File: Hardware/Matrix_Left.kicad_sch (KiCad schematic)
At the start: 0 parts

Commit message: Schematic review
Initial shcematic iteration.
Added all footprints and part numbers.
Only a quick review was performed.
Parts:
- added C13, C14, C15, C16, C17, C18, C19, C20, C21, C22, C23, C24, C25, C26, C27, C28, C29, C30, C31, C32, C33, C34, C35, C36, C37, C38, C39, C40, C41, C42, C43, C44, C45, C46, C47: 1u, Capacitor_SMD:C_0603_1608Metric, symbol Device:C
- added D10, D11, D17, D18, D19, D20, D21, D27, D28, D29, D30, D31, D37, D38, D39, D40, D41, D47, D48, D50, D51, D52, D57, D58, D60, D61, D62, D67, D68, D69, D7, D70, D71, D8, D9: SK6812MINI-E, LED_SMD:LED_SK6812MINI-E_3.2x2.8mm_P1.5mm_ReverseMount, symbol LED:SK6812MINI-E
- added D12, D13, D14, D15, D16, D22, D23, D24, D25, D26, D32, D33, D34, D35, D36, D42, D43, D44, D45, D46, D49, D53, D54, D55, D56, D59, D63, D64, D65, D66, D72, D73, D74, D75, D76: 1N4148WT, Diode_SMD:D_SOD-523, symbol Diode:1N4148WT
- added SW10, SW11, SW12, SW13, SW14, SW15, SW16, SW17, SW18, SW19, SW20, SW21, SW22, SW23, SW24, SW25, SW26, SW27, SW28, SW29, SW3, SW30, SW31, SW32, SW33, SW34, SW4, SW5, SW6, SW7, SW8, SW9: PG1350, Custom_Parts:PG1350_1.00u_PCB, symbol Switch:SW_Push
- added SW35: ENCODER, Custom_Parts:ALPS_EC11J_ENCODER, symbol Device:RotaryEncoder_Switch_MP
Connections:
- new net: D73.2 (A), SW32.2
- new net: D46.2 (A), SW22.2
- new net: D75.2 (A), SW34.2
- new net: D55.2 (A), SW25.2
- new net: D33.2 (A), SW14.2
- new net: D34.2 (A), SW15.2
- new net: D39.4 (DOUT), D50.2 (DIN)
- new net: D50.4 (DOUT), D60.2 (DIN)
- new net: D32.2 (A), SW13.2
- new net: D15.2 (A), SW6.2
- new net: D62.4 (DOUT), D71.2 (DIN)
- new net: D25.2 (A), SW11.2
- new net: D63.2 (A), SW27.2
- new net: D45.2 (A), SW21.2
- new net: D18.2 (DIN), D28.4 (DOUT)
- new net: D18.4 (DOUT), D8.2 (DIN)
- new net: D21.4 (DOUT), D31.2 (DIN)
- new net: D31.4 (DOUT), D41.2 (DIN)
- new net: D56.2 (A), SW26.2
- new net: D23.2 (A), SW9.2
- new net: D47.2 (DIN), D57.4 (DOUT)
- new net: D37.2 (DIN), D47.4 (DOUT)
- new net: D42.2 (A), SW18.2
- new net: D10.2 (DIN), D7.4 (DOUT)
- new net: D10.4 (DOUT), D20.2 (DIN)
- new net: D60.4 (DOUT), D69.2 (DIN)
- new net: D26.2 (A), SW12.2
- new net: D43.2 (A), SW19.2
- new net: D65.2 (A), SW29.2
- new net: D74.2 (A), SW33.2
- new net: D67.2 (DIN), D69.4 (DOUT)
- new net: D16.2 (A), SW7.2
- new net: D12.2 (A), SW3.2
- new net: D30.4 (DOUT), D40.2 (DIN)
- new net: D40.4 (DOUT), D51.2 (DIN)
- new net: D57.2 (DIN), D67.4 (DOUT)
- new net: D27.2 (DIN), D37.4 (DOUT)
- new net: D41.4 (DOUT), D52.2 (DIN)
- new net: D20.4 (DOUT), D30.2 (DIN)
- new net: D51.4 (DOUT), D61.2 (DIN)
- new net: D61.4 (DOUT), D70.2 (DIN)
- new net: D58.2 (DIN), D68.4 (DOUT)
- new net: D48.2 (DIN), D58.4 (DOUT)
- new net: D66.2 (A), SW30.2
- new net: D14.2 (A), SW5.2
- new net: D35.2 (A), SW16.2
- new net: D38.2 (DIN), D48.4 (DOUT)
- new net: D28.2 (DIN), D38.4 (DOUT)
- new net: D11.2 (DIN), D8.4 (DOUT)
- new net: D11.4 (DOUT), D21.2 (DIN)
- new net: D13.2 (A), SW4.2
- new net: D36.2 (A), SW17.2
- new net: D64.2 (A), SW28.2
- new net: D53.2 (A), SW23.2
- new net: D24.2 (A), SW10.2
- new net: D52.4 (DOUT), D62.2 (DIN)
- new net: D22.2 (A), SW8.2
- new net: D54.2 (A), SW24.2
- new net: D19.2 (DIN), D9.4 (DOUT)
- new net: D19.4 (DOUT), D29.2 (DIN)
- new net: D68.2 (DIN), D70.4 (DOUT)
- new net: D29.4 (DOUT), D39.2 (DIN)
- new net: D44.2 (A), SW20.2
- new net: D17.2 (DIN), D27.4 (DOUT)
- new net: D17.4 (DOUT), D7.2 (DIN)
- new net: D72.2 (A), SW31.2
- new net 5VL: C13.1, C14.1, C15.1, C16.1, C17.1, C18.1, C19.1, C20.1, C21.1, C22.1, C23.1, C24.1, C25.1, C26.1, C27.1, C28.1, C29.1, C30.1, C31.1, C32.1, C33.1, C34.1, C35.1, C36.1, C37.1, C38.1, C39.1, C40.1, C41.1, C42.1, C43.1, C44.1, C45.1, C46.1, C47.1, D10.3 (VDD), D11.3 (VDD), D17.3 (VDD), D18.3 (VDD), D19.3 (VDD), D20.3 (VDD), D21.3 (VDD), D27.3 (VDD), D28.3 (VDD), D29.3 (VDD), D30.3 (VDD), D31.3 (VDD), D37.3 (VDD), D38.3 (VDD), D39.3 (VDD), D40.3 (VDD), D41.3 (VDD), D47.3 (VDD), D48.3 (VDD), D50.3 (VDD), D51.3 (VDD), D52.3 (VDD), D57.3 (VDD), D58.3 (VDD), D60.3 (VDD), D61.3 (VDD), D62.3 (VDD), D67.3 (VDD), D68.3 (VDD), D69.3 (VDD), D7.3 (VDD), D70.3 (VDD), D71.3 (VDD), D8.3 (VDD), D9.3 (VDD)
- new net COL1_L: SW3.1, SW4.1, SW5.1, SW6.1, SW7.1
- new net COL2_L: SW10.1, SW11.1, SW12.1, SW8.1, SW9.1
- new net COL3_L: SW13.1, SW14.1, SW15.1, SW16.1, SW17.1
- new net COL4_L: SW18.1, SW19.1, SW20.1, SW21.1, SW22.1
- new net COL5_L: D49.2 (A), SW23.1, SW24.1, SW25.1, SW26.1
- new net COL6_L: D59.2 (A), SW27.1, SW28.1, SW29.1, SW30.1
- new net COL7_L: SW31.1, SW32.1, SW33.1, SW34.1, SW35.S1
- new net ENC_CC: D59.1 (K), SW35.B
- new net ENC_CW: D49.1 (K), SW35.A
- new net ENC_SW: D76.2 (A), SW35.S2
- new net GND: C13.2, C14.2, C15.2, C16.2, C17.2, C18.2, C19.2, C20.2, C21.2, C22.2, C23.2, C24.2, C25.2, C26.2, C27.2, C28.2, C29.2, C30.2, C31.2, C32.2, C33.2, C34.2, C35.2, C36.2, C37.2, C38.2, C39.2, C40.2, C41.2, C42.2, C43.2, C44.2, C45.2, C46.2, C47.2, D10.1 (VSS), D11.1 (VSS), D17.1 (VSS), D18.1 (VSS), D19.1 (VSS), D20.1 (VSS), D21.1 (VSS), D27.1 (VSS), D28.1 (VSS), D29.1 (VSS), D30.1 (VSS), D31.1 (VSS), D37.1 (VSS), D38.1 (VSS), D39.1 (VSS), D40.1 (VSS), D41.1 (VSS), D47.1 (VSS), D48.1 (VSS), D50.1 (VSS), D51.1 (VSS), D52.1 (VSS), D57.1 (VSS), D58.1 (VSS), D60.1 (VSS), D61.1 (VSS), D62.1 (VSS), D67.1 (VSS), D68.1 (VSS), D69.1 (VSS), D7.1 (VSS), D70.1 (VSS), D71.1 (VSS), D8.1 (VSS), D9.1 (VSS), SW35.MP
- new net LED_DATA_L: D9.2 (DIN)
- new net ROW1_L: D12.1 (K), D22.1 (K), D32.1 (K), D42.1 (K), D53.1 (K), D63.1 (K), D72.1 (K)
- new net ROW2_L: D13.1 (K), D23.1 (K), D33.1 (K), D43.1 (K), D54.1 (K), D64.1 (K), D73.1 (K)
- new net ROW3_L: D14.1 (K), D24.1 (K), D34.1 (K), D44.1 (K), D55.1 (K), D65.1 (K), D74.1 (K)
- new net ROW4_L: D15.1 (K), D25.1 (K), D35.1 (K), D45.1 (K), D56.1 (K), D66.1 (K), D75.1 (K)
- new net ROW5_L: D16.1 (K), D26.1 (K), D36.1 (K), D46.1 (K), D76.1 (K), SW35.C
- no-connect marks 0 -> 1

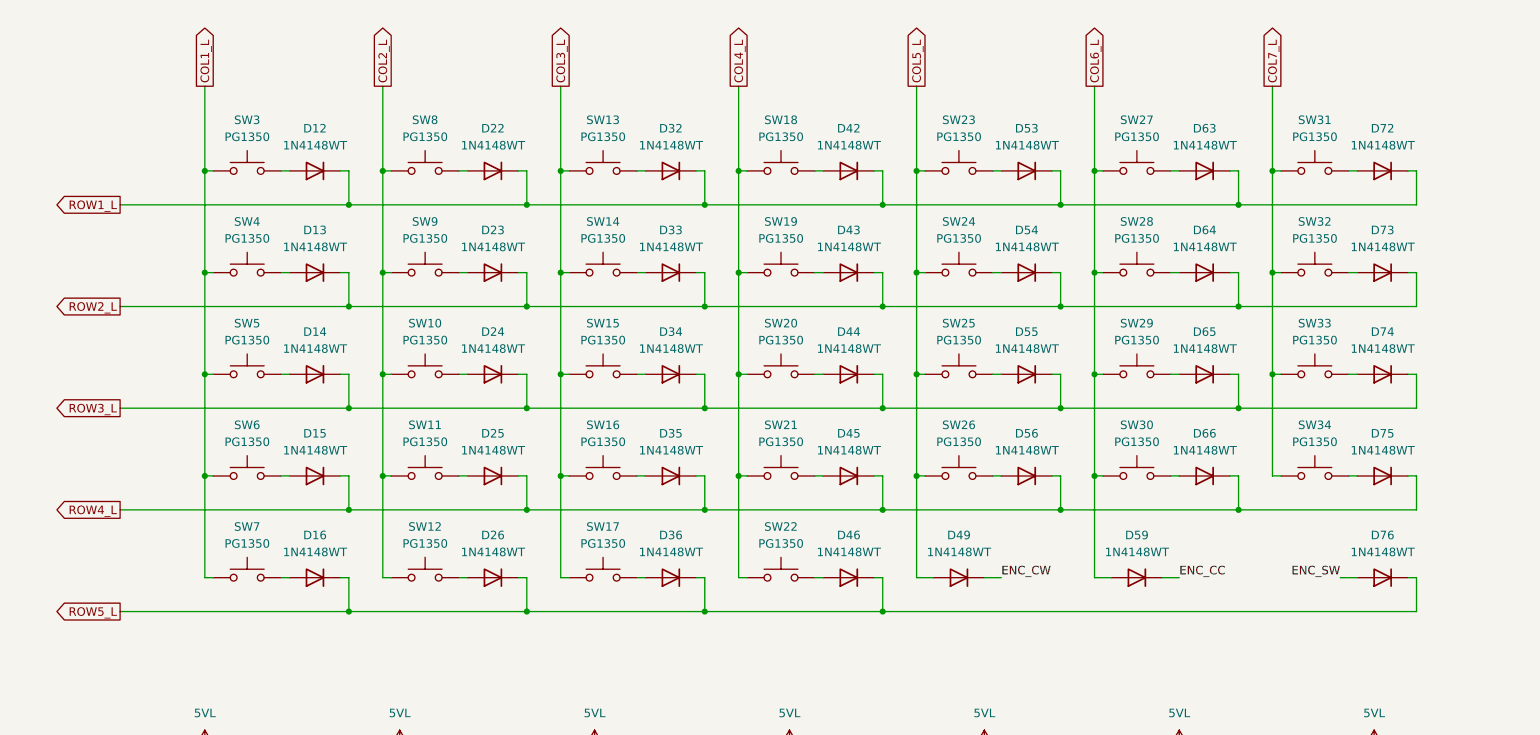
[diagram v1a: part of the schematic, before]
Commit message: Net configurations
Added net labels.
Updated the PCB components.
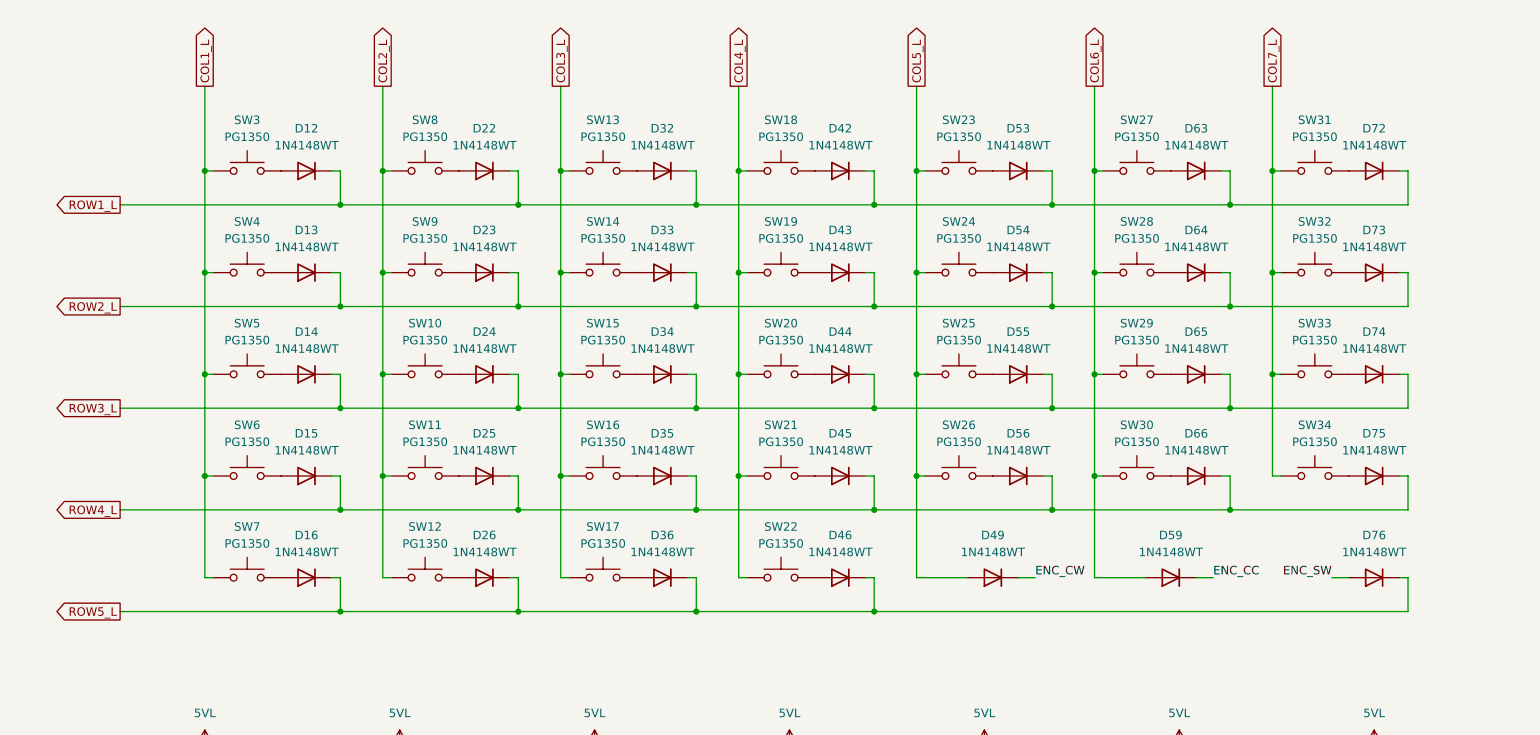
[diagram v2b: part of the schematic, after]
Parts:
- D10, D11, D17, D18, D19, D20, D21, D27, D28, D29, D30, D31, D37, D38, D39, D40, D41, D47, D48, D50, D51, D52, D57, D58, D60, D61, D62, D67, D68, D69, D7, D70, D71, D8, D9: footprint LED_SMD:LED_SK6812MINI-E_3.2x2.8mm_P1.5mm_ReverseMount -> Custom_Parts:LED_SK6812MINI-E_3.2x2.8mm_P1.5mm_ReverseMount
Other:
- moved on the sheet: D12, D13, D14, D15, D16, D22, D23, D24, D25, D26, D32, D33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

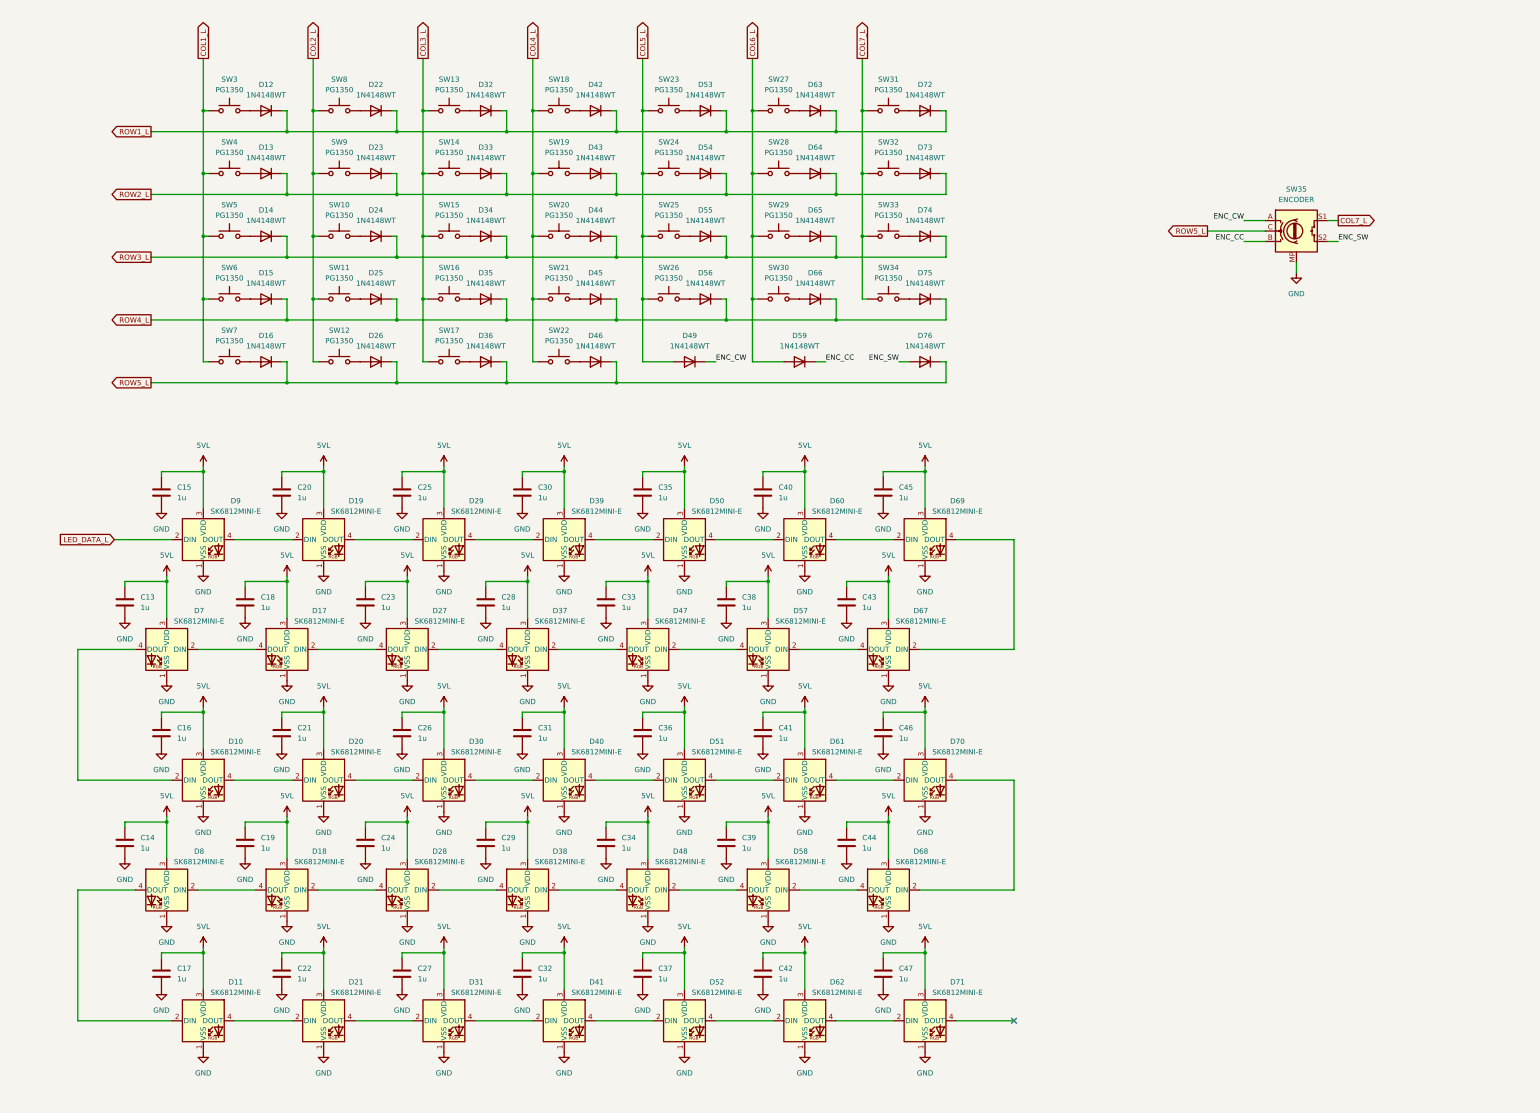
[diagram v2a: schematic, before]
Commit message: Initial layout
Configured the switch and LED initial layout.
Need to add the capacitors for the LEDs and the diodes for the switches.
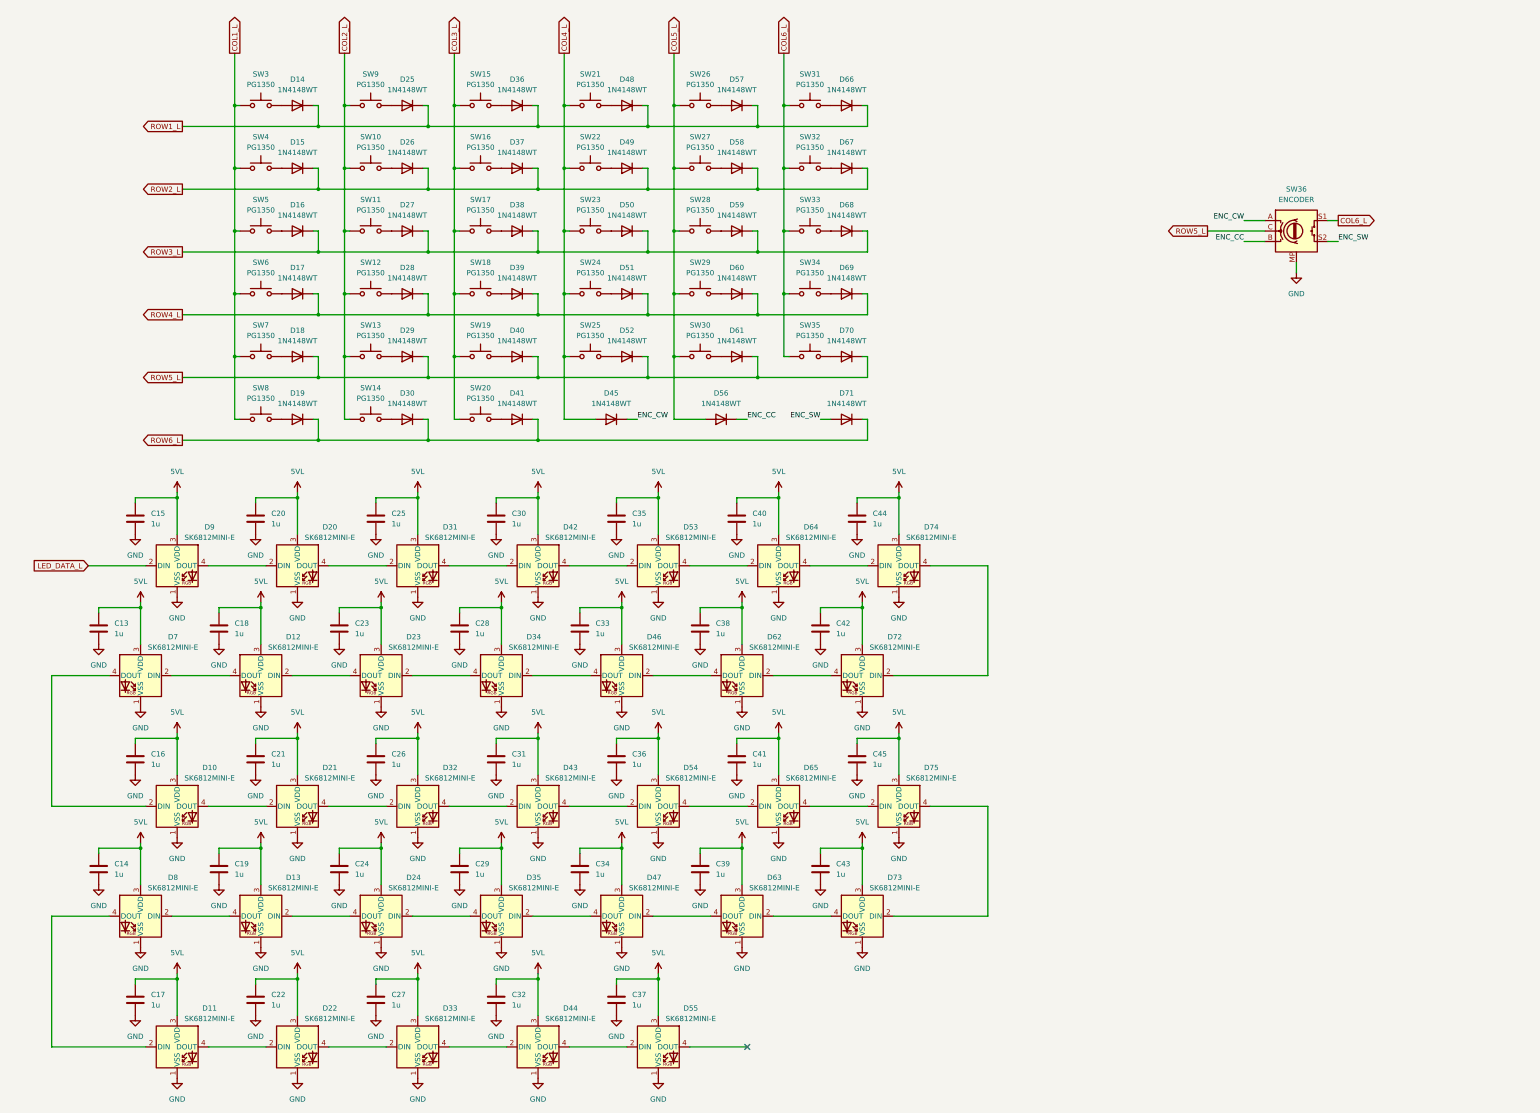
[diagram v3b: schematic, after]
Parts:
- removed C42, C47: 1u, Capacitor_SMD:C_0603_1608Metric, symbol Device:C
- removed D46, D49, D59, D72, D73, D74, D75, D76: 1N4148WT, Diode_SMD:D_SOD-523, symbol Diode:1N4148WT
- removed D62, D71: SK6812MINI-E, Custom_Parts:LED_SK6812MINI-E_3.2x2.8mm_P1.5mm_ReverseMount, symbol LED:SK6812MINI-E
- removed SW22, SW31, SW32, SW33, SW34: PG1350, Custom_Parts:PG1350_1.00u_PCB, symbol Switch:SW_Push
- added D18, D29, D40, D45, D52, D56, D61, D70, D71: 1N4148WT, Diode_SMD:D_SOD-523, symbol Diode:1N4148WT
- added SW13, SW19, SW25, SW30, SW35, SW7: PG1350, Custom_Parts:PG1350_1.00u_PCB, symbol Switch:SW_Push
- renumbered C43 to C42, C44 to C43, C45 to C44, C46 to C45, D17 to D12, D18 to D13, D12 to D14, D13 to D15, D14 to D16, D15 to D17, D16 to D19, D19 to D20, D20 to D21, D21 to D22, D27 to D23, D28 to D24, D22 to D25, D23 to D26, D24 to D27, D25 to D28, D26 to D30, D29 to D31, D30 to D32, D31 to D33, D37 to D34, D38 to D35, D32 to D36, D33 to D37, D34 to D38, D35 to D39, D36 to D41, D39 to D42, D40 to D43, D41 to D44, D47 to D46, D48 to D47, D42 to D48, D43 to D49, D44 to D50, D45 to D51, D50 to D53, D51 to D54, D52 to D55, D53 to D57, D54 to D58, D55 to D59, D56 to D60, D57 to D62, D58 to D63, D60 to D64, D61 to D65, D63 to D66, D64 to D67, D65 to D68, D66 to D69, D67 to D72, D68 to D73, D69 to D74, D70 to D75, SW9 to SW10, SW10 to SW11, SW11 to SW12, SW12 to SW14, SW13 to SW15, SW14 to SW16, SW15 to SW17, SW16 to SW18, SW17 to SW20, SW18 to SW21, SW19 to SW22, SW20 to SW23, SW21 to SW24, SW23 to SW26, SW24 to SW27, SW25 to SW28, SW26 to SW29, SW27 to SW31, SW28 to SW32, SW29 to SW33, SW30 to SW34, SW35 to SW36, SW7 to SW8, SW8 to SW9
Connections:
- net COL7_L is gone; now on net COL6_L: SW36.S1
- net COL1_L: now also SW7.1
- net COL2_L: now also SW13.1
- net COL3_L: now also SW19.1
- net COL4_L: now also D45.2 (A), SW25.1
- net COL5_L: now also D56.2 (A), SW30.1
- net COL6_L: now also SW35.1
- net ENC_CC: now also D56.1 (K)
- net ENC_CW: now also D45.1 (K)
- net ENC_SW: now also D71.2 (A)
- net ROW5_L: now also D18.1 (K), D29.1 (K), D40.1 (K), D52.1 (K), D61.1 (K), D70.1 (K); no longer D19.1 (K), D30.1 (K), D41.1 (K)
- new net: D70.2 (A), SW35.2
- new net: D52.2 (A), SW25.2
- new net: D40.2 (A), SW19.2
- new net: D18.2 (A), SW7.2
- new net: D29.2 (A), SW13.2
- new net: D61.2 (A), SW30.2
- new net ROW6_L: D19.1 (K), D30.1 (K), D41.1 (K), D71.1 (K)
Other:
- moved on the sheet: C13, C14, C15, C16, C17, C18, C19, C20, C21, C22, C23, C24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

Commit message: Pin adjustment
Adjusted the pins for the encoders and other.
Now the battery measuring pin connected to an internal ADC on the XIAO nRF52840 also serves to read the rotation of the encoders.
Attention should be put as how to implement the BAT voltage measuring to check if the encoder is turning at the same time.
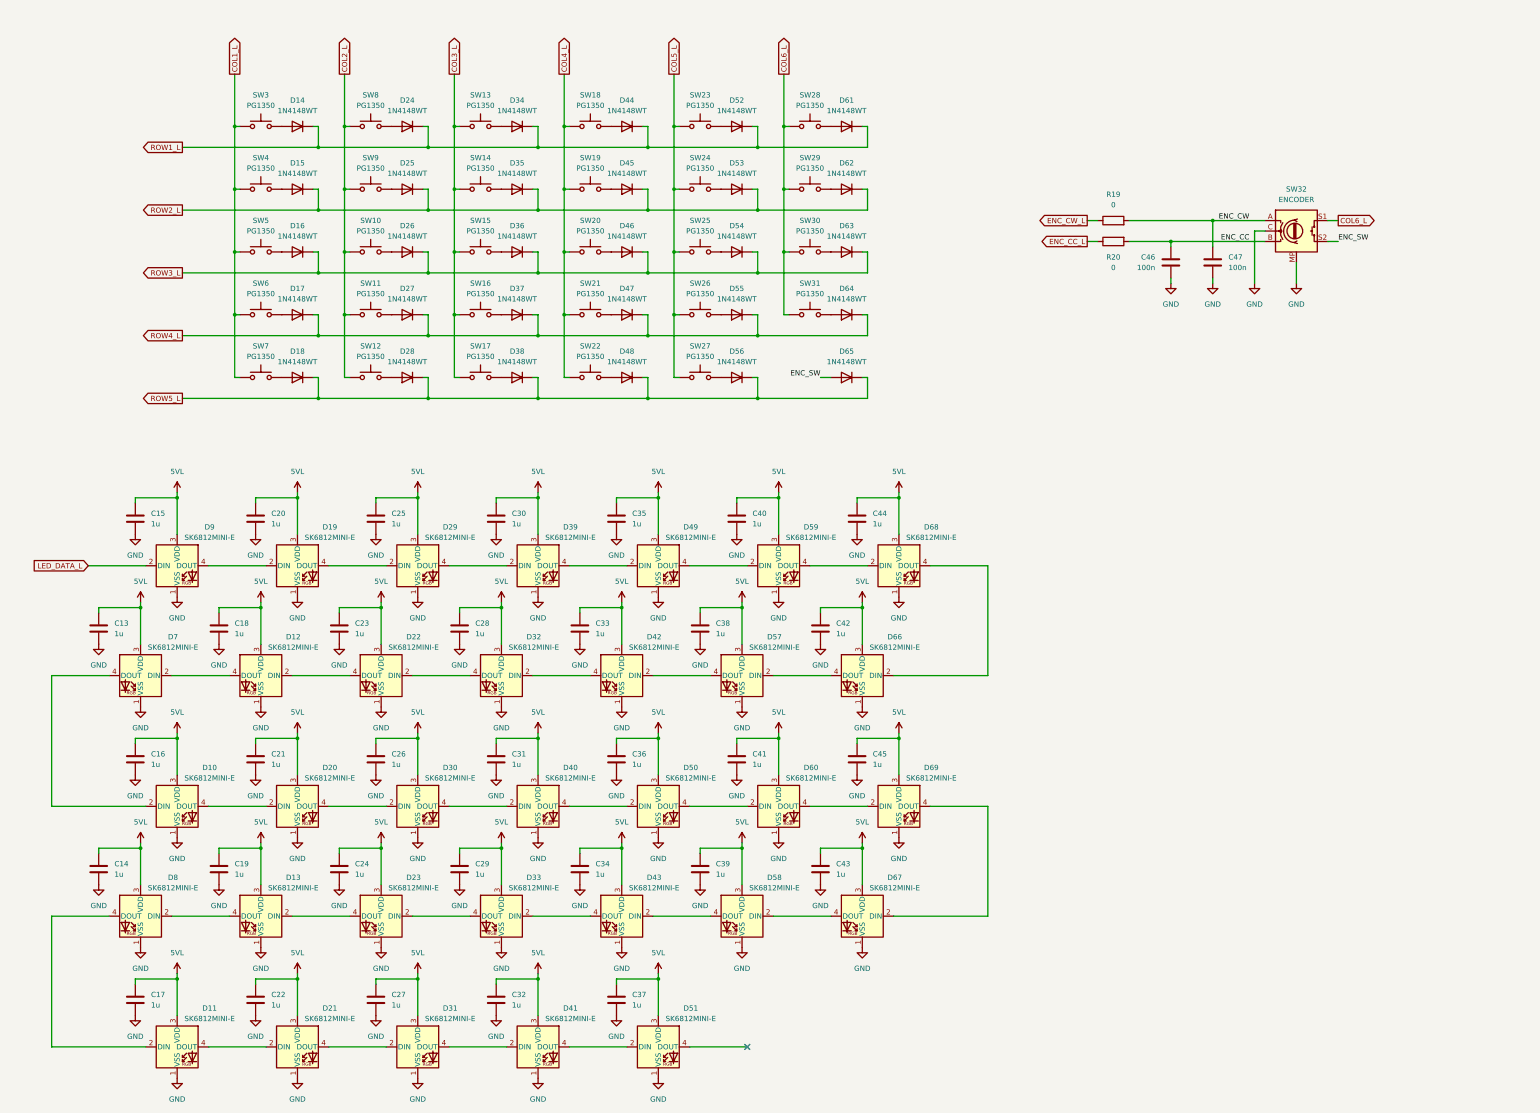
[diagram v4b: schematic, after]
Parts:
- removed D19, D30, D41, D45, D56, D71: 1N4148WT, Diode_SMD:D_SOD-523, symbol Diode:1N4148WT
- removed SW14, SW20, SW35, SW8: PG1350, Custom_Parts:PG1350_1.00u_PCB, symbol Switch:SW_Push
- added C46, C47: 100n, Capacitor_SMD:C_0603_1608Metric, symbol Device:C
- added R19, R20: 0, Resistor_SMD:R_0603_1608Metric, symbol Device:R
- renumbered D20 to D19, D21 to D20, D22 to D21, D23 to D22, D24 to D23, D25 to D24, D26 to D25, D27 to D26, D28 to D27, D29 to D28, D31 to D29, D32 to D30, D33 to D31, D34 to D32, D35 to D33, D36 to D34, D37 to D35, D38 to D36, D39 to D37, D40 to D38, D42 to D39, D43 to D40, D44 to D41, D46 to D42, D47 to D43, D48 to D44, D49 to D45, D50 to D46, D51 to D47, D52 to D48, D53 to D49, D54 to D50, D55 to D51, D57 to D52, D58 to D53, D59 to D54, D60 to D55, D61 to D56, D62 to D57, D63 to D58, D64 to D59, D65 to D60, D66 to D61, D67 to D62, D68 to D63, D69 to D64, D70 to D65, D72 to D66, D73 to D67, D74 to D68, D75 to D69, SW11 to SW10, SW12 to SW11, SW13 to SW12, SW15 to SW13, SW16 to SW14, SW17 to SW15, SW18 to SW16, SW19 to SW17, SW21 to SW18, SW22 to SW19, SW23 to SW20, SW24 to SW21, SW25 to SW22, SW26 to SW23, SW27 to SW24, SW28 to SW25, SW29 to SW26, SW30 to SW27, SW31 to SW28, SW32 to SW29, SW33 to SW30, SW34 to SW31, SW36 to SW32, SW9 to SW8, SW10 to SW9
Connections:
- net ENC_CC: now also C46.1, R20.2
- net ENC_CW: now also C47.1, R19.2
- net ENC_SW: now also D65.2 (A)
- net GND: now also SW32.C, C46.2, C47.2
- net ROW5_L: no longer SW32.C
- new net ENC_CC_L: R20.1
- new net ENC_CW_L: R19.1
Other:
- moved on the sheet: D14, D15, D16, D17, D18, D24, D25, D26, D27, D28, D34, D35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
